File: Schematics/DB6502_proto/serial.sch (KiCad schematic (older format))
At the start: 22 parts, among them J11 LCD Port, J12 VIA Ports, J13 UART GPIO, U17 74AC08, U18 SC26C92, U19 65C22S, U20 74AC04, U21 74AC574, U8 74AC04, U9 74HC21, Y2 3,6864MHz

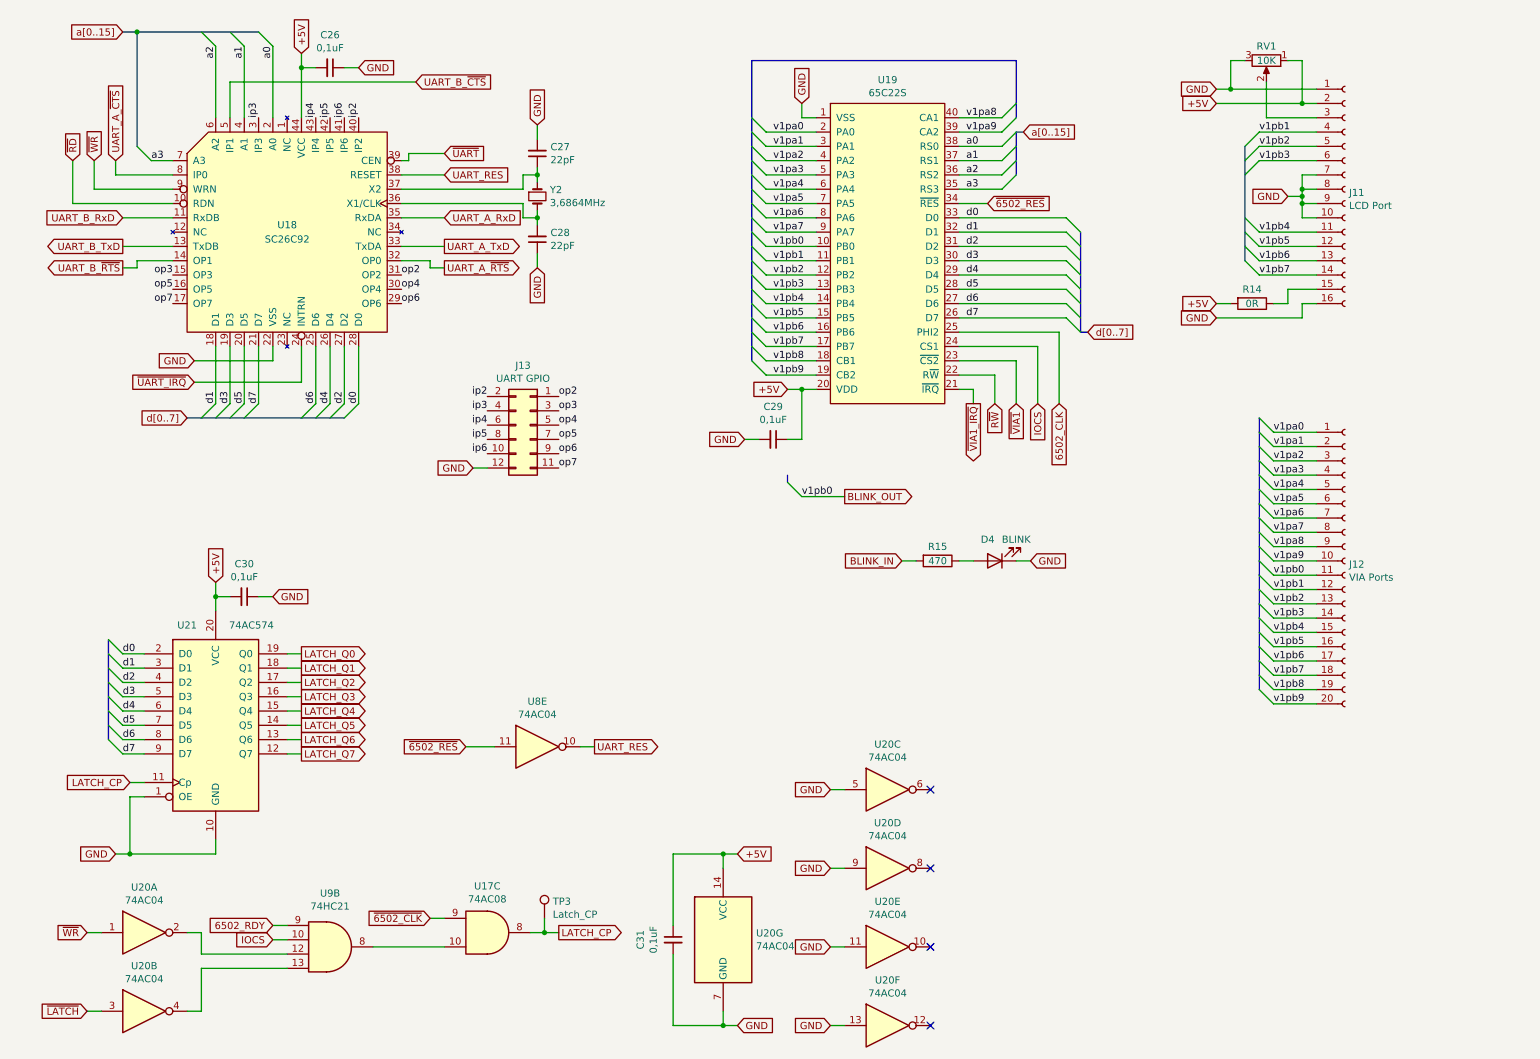
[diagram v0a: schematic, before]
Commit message: Working on massively redesigned board
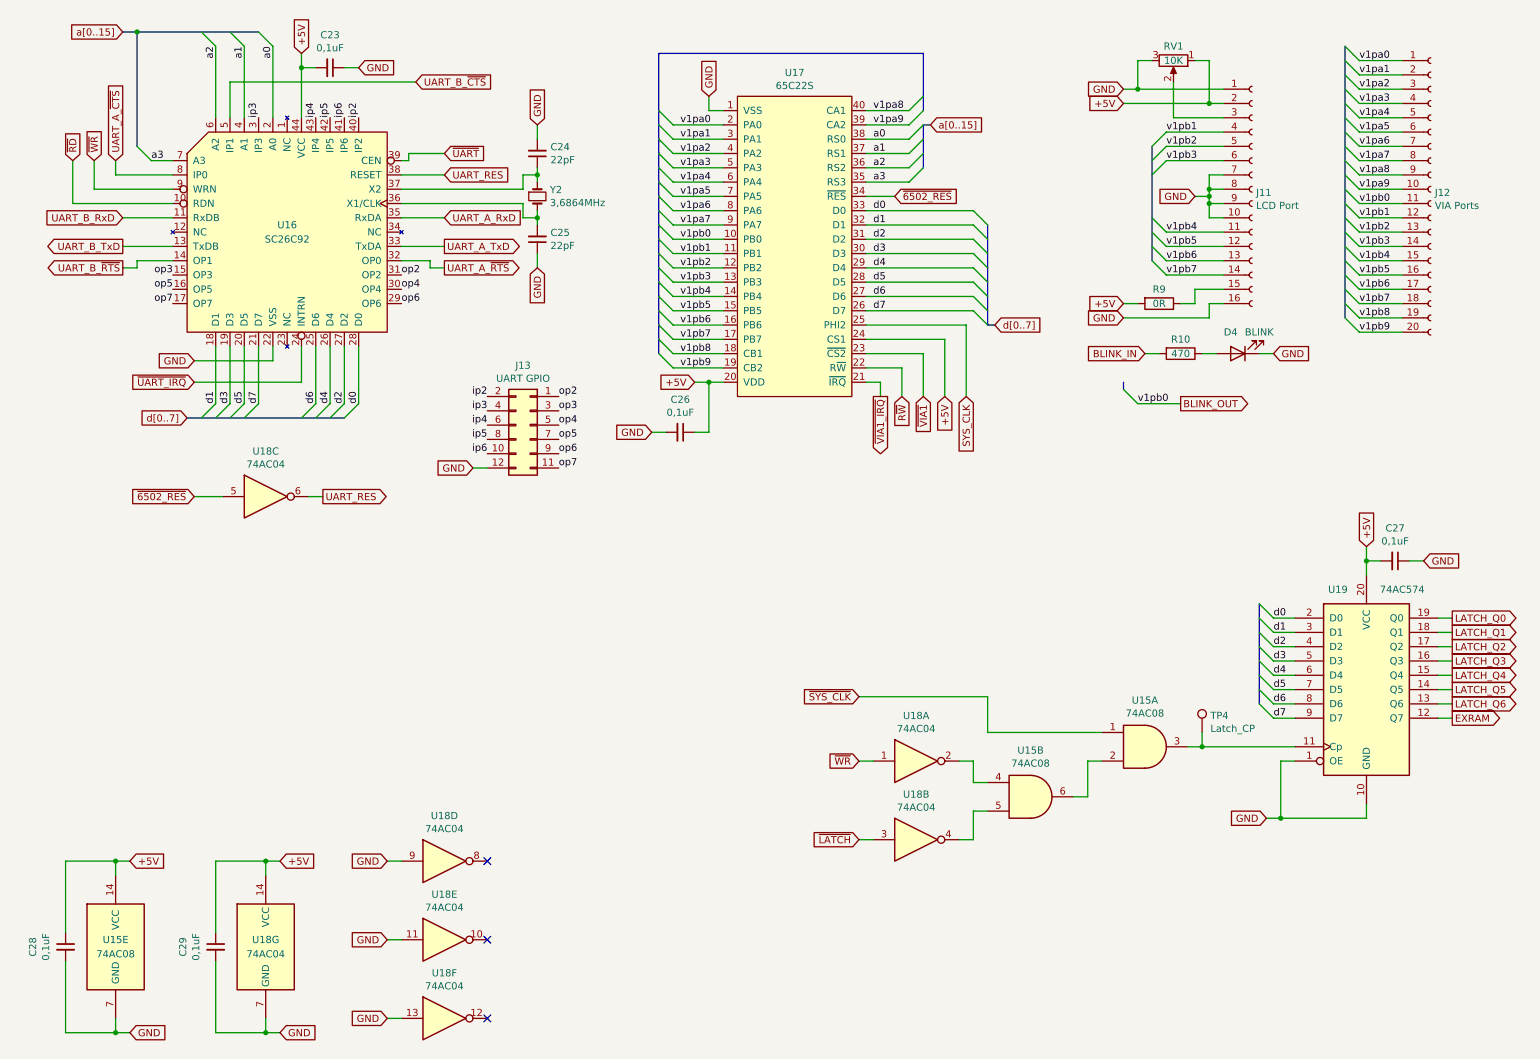
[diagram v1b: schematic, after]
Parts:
- removed unit 3 of U20
- removed U8: 74AC04, Package_SO:SOIC-14_3.9x8.7mm_P1.27mm, symbol 74xx:74LS04
- removed U9: 74HC21, Package_SO:SOIC-14_3.9x8.7mm_P1.27mm, symbol 74xx:74LS21
- added C28: 0,1uF, Capacitor_SMD:C_1206_3216Metric_Pad1.33x1.80mm_HandSolder, symbol Device:C_Small
- added unit 2 of U15
- added unit 5 of U15
- added unit 3 of U18
- C23: renamed from C26; footprint Capacitor_SMD:C_1206_3216Metric_Pad1.42x1.75mm_HandSolder -> Capacitor_SMD:C_1206_3216Metric_Pad1.33x1.80mm_HandSolder
- C26: renamed from C29; footprint Capacitor_SMD:C_1206_3216Metric_Pad1.42x1.75mm_HandSolder -> Capacitor_SMD:C_1206_3216Metric_Pad1.33x1.80mm_HandSolder
- C27: renamed from C30; footprint Capacitor_SMD:C_1206_3216Metric_Pad1.42x1.75mm_HandSolder -> Capacitor_SMD:C_1206_3216Metric_Pad1.33x1.80mm_HandSolder
- C29: renamed from C31; footprint Capacitor_SMD:C_1206_3216Metric_Pad1.42x1.75mm_HandSolder -> Capacitor_SMD:C_1206_3216Metric_Pad1.33x1.80mm_HandSolder
- R10: renamed from R15; footprint Resistor_SMD:R_1206_3216Metric_Pad1.42x1.75mm_HandSolder -> Resistor_SMD:R_1206_3216Metric_Pad1.30x1.75mm_HandSolder
- renumbered C27 to C24, C28 to C25, R14 to R9, TP3 to TP4, U17 to U15, U18 to U16, U19 to U17, U20 to U18, U21 to U19
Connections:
- net IOCS is gone; now on net +5V: U17.24 (CS1)
- net +5V: now also C28.1, U15.14 (VCC)
- net GND: now also C28.2, U15.7 (GND)
- net UART_RES: now also U18.6
- net ~6502_RES: now also U18.5
- net at U18.2: now also U15.4
- net at U18.4: now also U15.5
- net 6502_CLK renamed SYS_CLK
- net LATCH_CP: no longer names the net of TP4.1, U19.11 (Cp)
- net LATCH_CP: now also U15.3; no longer U15.8
- net LATCH_Q7 renamed EXRAM
- removed net ~6502_CLK: U15.9
- new net: U15.2, U15.6
- new net ~SYS_CLK: U15.1
- no-connect marks 4 -> 3
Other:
- moved on the sheet: C26, C27, C29, D4, J11, J12, R10, R9, RV1, TP4, U17, U18A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
